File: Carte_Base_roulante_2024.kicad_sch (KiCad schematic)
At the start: 64 parts, among them J11 ENCA, J16 ALIM, J4 ENCB, J5 ENCC, Q2 IRF7424, U1 STM32G484RETx

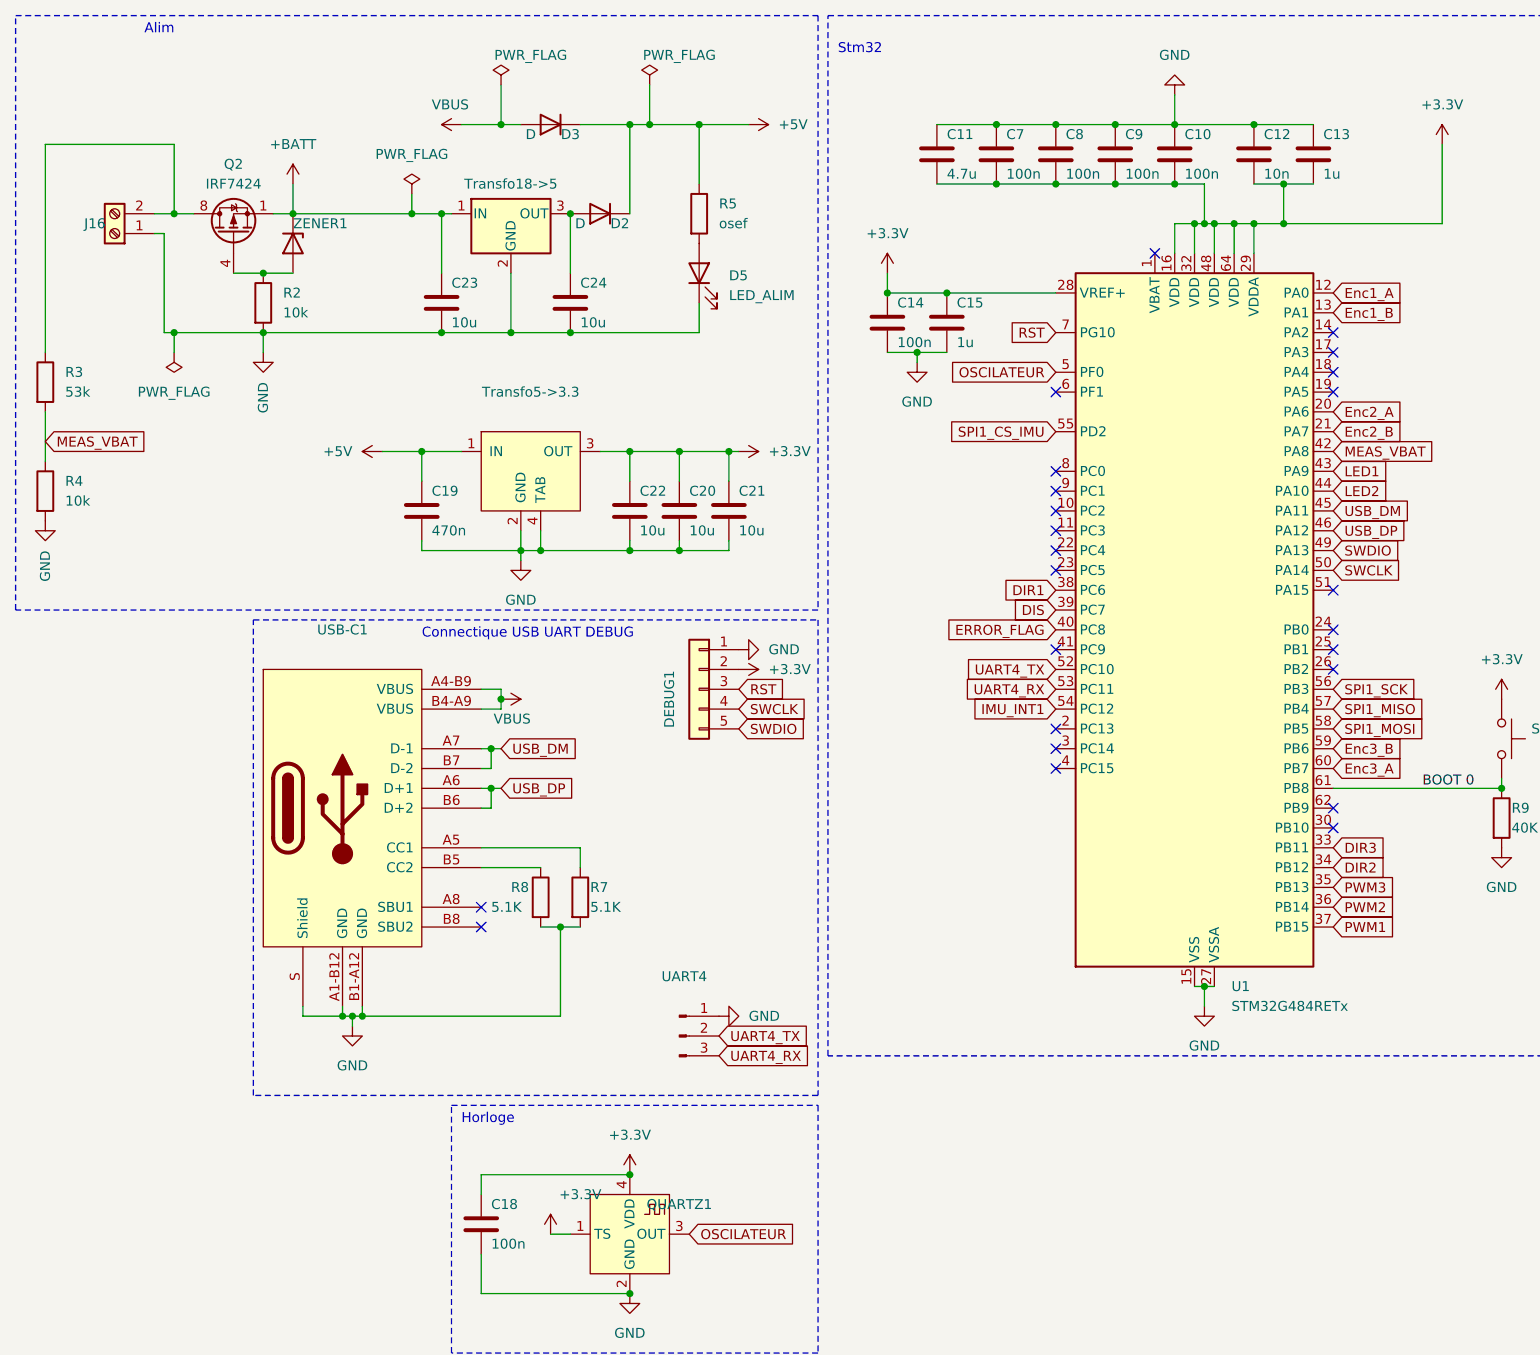
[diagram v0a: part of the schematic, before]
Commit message: routage avançé
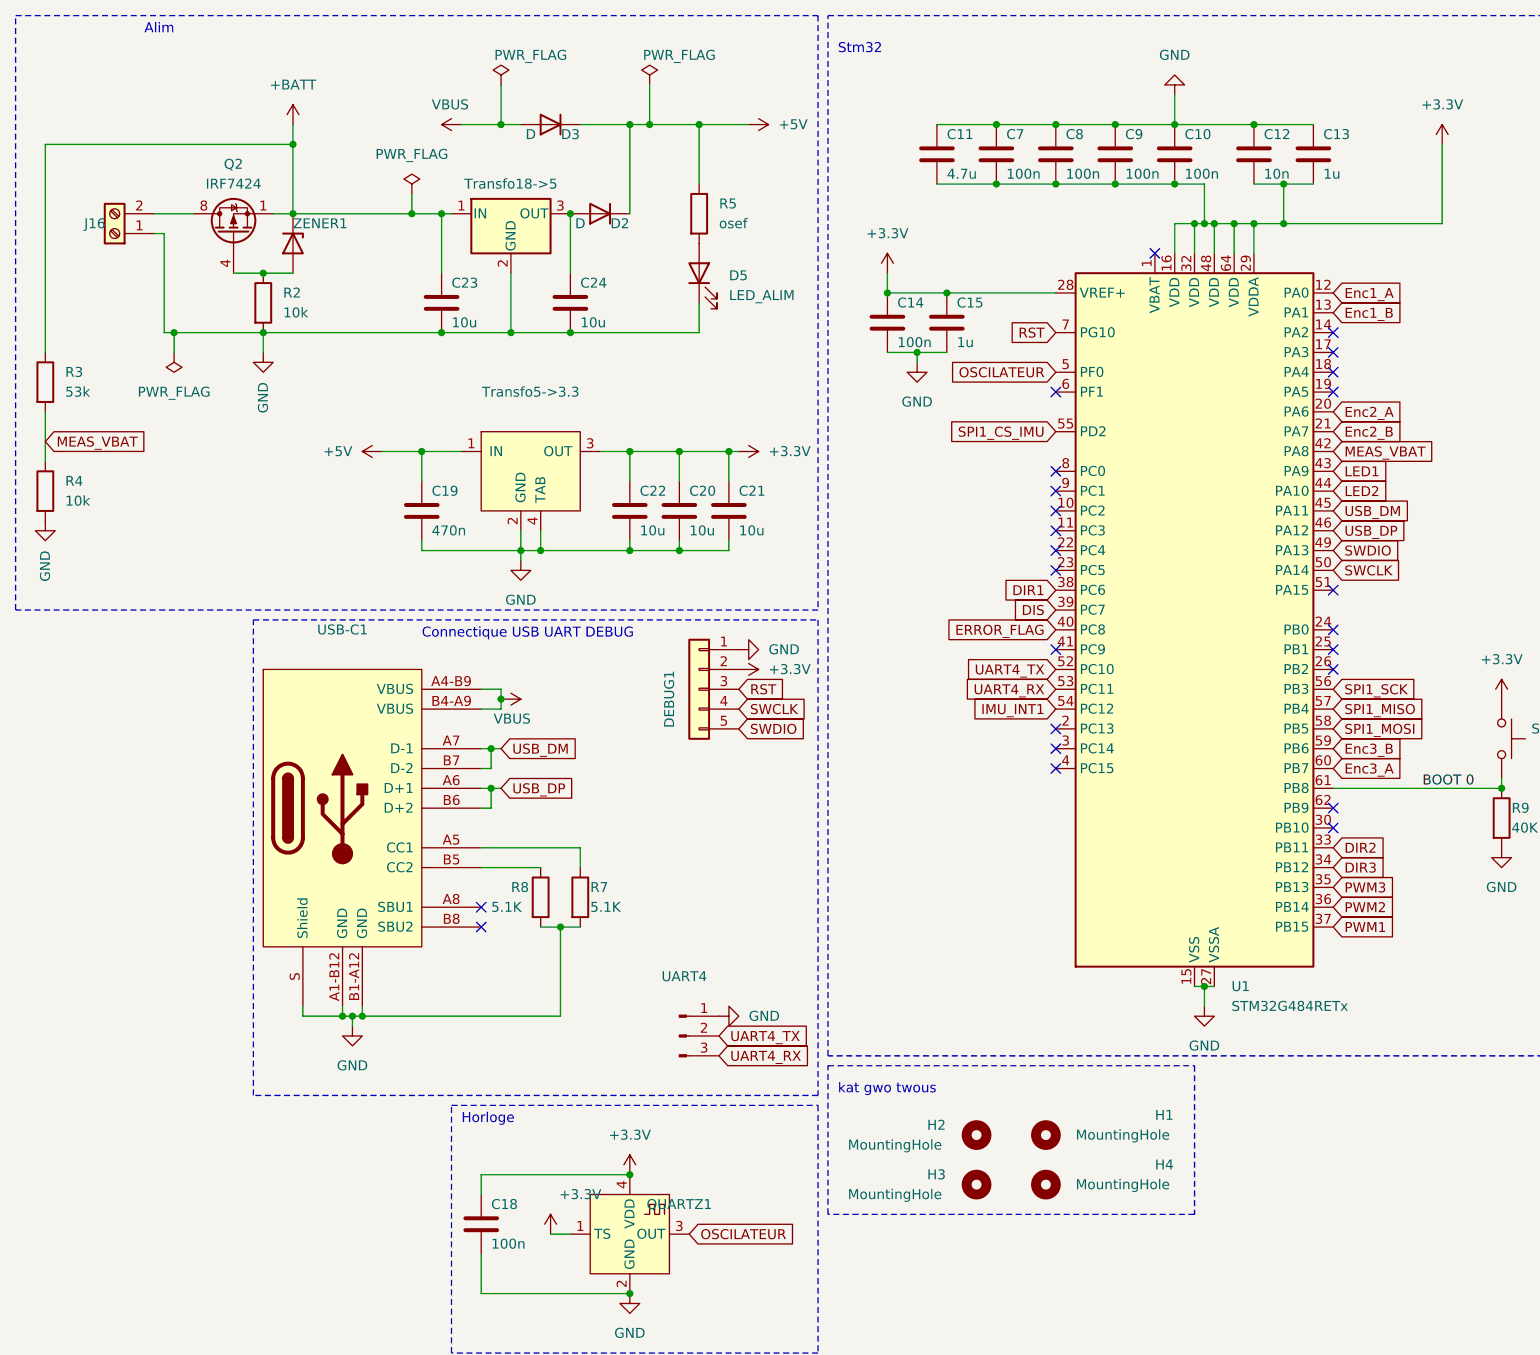
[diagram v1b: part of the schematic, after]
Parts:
- added H1, H2, H3, H4: MountingHole, MountingHole:MountingHole_3.2mm_M3, symbol Mechanical:MountingHole
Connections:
- net +BATT: now also R3.1
- net DIR2: now also U1.33 (PB11); no longer U1.34 (PB12)
- net DIR3: now also U1.34 (PB12); no longer U1.33 (PB11)
- net at J16.2 (Pin_2), Q2.5 (D), Q2.6 (D)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: no longer R3.1
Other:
- note added: "kat gwo twous"
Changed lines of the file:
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@@
   (junction (at 173.99 45.72) (diameter 0) (color 0 0 0 0)
   )
-  (junction (at 35.56 44.45) (diameter 0) (color 0 0 0 0)
-  )
   (junction (at 93.98 167.64) (diameter 0) (color 0 0 0 0)
   )
@@
   (junction (at 336.55 29.21) (diameter 0) (color 0 0 0 0)
   )
+  (junction (at 50.8 35.56) (diameter 0) (color 0 0 0 0)
+  )
   (junction (at 93.98 182.88) (diameter 0) (color 0 0 0 0)
   )
@@
     (stroke (width 0) (type default))
   )
+  (wire (pts (xy 19.05 35.56) (xy 50.8 35.56))
+    (stroke (width 0) (type default))
+  )
   (wire (pts (xy 86.36 44.45) (xy 86.36 52.07))
     (stroke (width 0) (type default))
@@
     (stroke (width 0) (type default))
   )
-  (wire (pts (xy 35.56 44.45) (xy 38.1 44.45))
+  (wire (pts (xy 33.02 44.45) (xy 38.1 44.45))
     (stroke (width 0) (type default))
   )
@@
     (stroke (width 0) (type default))
   )
-  (wire (pts (xy 19.05 35.56) (xy 35.56 35.56))
-    (stroke (width 0) (type default))
-  )
   (wire (pts (xy 254 36.83) (xy 255.27 36.83))
     (stroke (width 0) (type default))
@@
     (stroke (width 0) (type default))
   )
-  (wire (pts (xy 35.56 35.56) (xy 35.56 44.45))
-    (stroke (width 0) (type default))
-  )
   (wire (pts (xy 311.15 57.15) (xy 307.34 57.15))
     (stroke (width 0) (type default))
@@
     (stroke (width 0) (type default))
   )
+  (wire (pts (xy 50.8 35.56) (xy 50.8 44.45))
+    (stroke (width 0) (type default))
+  )
+  (wire (pts (xy 19.05 62.23) (xy 19.05 35.56))
+    (stroke (width 0) (type default))
+  )
   (wire (pts (xy 336.55 127) (xy 346.71 127))
     (stroke (width 0) (type default))
@@
     (stroke (width 0) (type default))
   )
-  (wire (pts (xy 33.02 44.45) (xy 35.56 44.45))
-    (stroke (width 0) (type default))
-  )
   (wire (pts (xy 163.83 45.72) (xy 166.37 45.72))
     (stroke (width 0) (type default))
@@
     (stroke (width 0) (type default))
   )
-  (wire (pts (xy 50.8 40.64) (xy 50.8 44.45))
+  (wire (pts (xy 50.8 33.02) (xy 50.8 35.56))
     (stroke (width 0) (type default))
   )
@@
     (stroke (width 0) (type default))
   )
-  (wire (pts (xy 19.05 35.56) (xy 19.05 62.23))
-    (stroke (width 0) (type default))
-  )
   (wire (pts (xy 177.8 45.72) (xy 173.99 45.72))
     (stroke (width 0) (type default))
@@
     (fill (type none))
   )
+  (rectangle (start 119.38 153.67) (end 166.37 172.72)
+    (stroke (width 0) (type dash))
+    (fill (type none))
+  )
   (rectangle (start 220.98 101.6) (end 283.21 130.81)
     (stroke (width 0) (type dash))
@@
     (effects (font (size 2 2)) (justify left bottom))
   )
+  (text "kat gwo twous\n" (at 120.65 157.48 0)
+    (effects (font (size 1.27 1.27)) (justify left bottom))
+  )
   (text "Encodeurs Moteurs" (at 222.25 81.28 0)
     (effects (font (size 1.27 1.27)) (justify left bottom))
@@
     )
   )
-  (global_label "DIR3" (shape input) (at 184.15 125.73 0) (fields_autoplaced)
+  (global_label "DIR3" (shape input) (at 184.15 128.27 0) (fields_autoplaced)
     (effects (font (size 1.27 1.27)) (justify left))
-    (property "Intersheetrefs" "${INTERSHEET_REFS}" (at 191.4895 125.73 0)
+    (property "Intersheetrefs" "${INTERSHEET_REFS}" (at 191.4895 128.27 0)
       (effects (font (size 1.27 1.27)) (justify left) hide)
     )
@@
     )
   )
-  (global_label "DIR2" (shape input) (at 184.15 128.27 0) (fields_autoplaced)
+  (global_label "DIR2" (shape input) (at 184.15 125.73 0) (fields_autoplaced)
     (effects (font (size 1.27 1.27)) (justify left))
-    (property "Intersheetrefs" "${INTERSHEET_REFS}" (at 191.4895 128.27 0)
+    (property "Intersheetrefs" "${INTERSHEET_REFS}" (at 191.4895 125.73 0)
       (effects (font (size 1.27 1.27)) (justify left) hide)
     )
@@
     )
   )
+  (symbol (lib_id "Mechanical:MountingHole") (at 147.32 168.91 0) (unit 1)
+    (in_bom yes) (on_board yes) (dnp no)
+    (property "Reference" "H4" (at 161.29 166.37 0)
+      (effects (font (size 1.27 1.27)) (justify left))
+    )
+    (property "Value" "MountingHole" (at 151.13 168.91 0)
+      (effects (font (size 1.27 1.27)) (justify left))
+    )
+    (property "Footprint" "MountingHole:MountingHole_3.2mm_M3" (at 147.32 168.91 0)
+      (effects (font (size 1.27 1.27)) hide)
+    )
+    (property "Datasheet" "~" (at 147.32 168.91 0)
+      (effects (font (size 1.27 1.27)) hide)
+    )
+    (instances
+      (project "Carte_Base_roulante_2024"
+        (path "/f941aee9-3a44-439b-9c30-032c53e86031"
+          (reference "H4") (unit 1)
+        )
+      )
+    )
+  )
   (symbol (lib_id "power:+5V") (at 231.14 90.17 90) (mirror x) (unit 1)
     (in_bom yes) (on_board yes) (dnp no) (fields_autoplaced)
@@
     )
   )
+  (symbol (lib_id "Mechanical:MountingHole") (at 147.32 162.56 0) (unit 1)
+    (in_bom yes) (on_board yes) (dnp no)
+    (property "Reference" "H1" (at 161.29 160.02 0)
+      (effects (font (size 1.27 1.27)) (justify left))
+    )
+    (property "Value" "MountingHole" (at 151.13 162.56 0)
+      (effects (font (size 1.27 1.27)) (justify left))
+    )
+    (property "Footprint" "MountingHole:MountingHole_3.2mm_M3" (at 147.32 162.56 0)
+      (effects (font (size 1.27 1.27)) hide)
+    )
+    (property "Datasheet" "~" (at 147.32 162.56 0)
+      (effects (font (size 1.27 1.27)) hide)
+    )
+    (instances
+      (project "Carte_Base_roulante_2024"
+        (path "/f941aee9-3a44-439b-9c30-032c53e86031"
+          (reference "H1") (unit 1)
+        )
+      )
+    )
+  )
   (symbol (lib_id "Device:C") (at 67.31 82.55 0) (unit 1)
     (in_bom yes) (on_board yes) (dnp no)
@@
     )
   )
-  (symbol (lib_id "power:+BATT") (at 50.8 40.64 0) (unit 1)
+  (symbol (lib_id "power:+BATT") (at 50.8 33.02 0) (unit 1)
     (in_bom yes) (on_board yes) (dnp no) (fields_autoplaced)
-    (property "Reference" "#PWR029" (at 50.8 44.45 0)
+    (property "Reference" "#PWR029" (at 50.8 36.83 0)
       (effects (font (size 1.27 1.27)) hide)
     )
-    (property "Value" "+BATT" (at 50.8 35.56 0)
+    (property "Value" "+BATT" (at 50.8 27.94 0)
       (effects (font (size 1.27 1.27)))
     )
-    (property "Footprint" "" (at 50.8 40.64 0)
+    (property "Footprint" "" (at 50.8 33.02 0)
       (effects (font (size 1.27 1.27)) hide)
     )
-    (property "Datasheet" "" (at 50.8 40.64 0)
+    (property "Datasheet" "" (at 50.8 33.02 0)
       (effects (font (size 1.27 1.27)) hide)
     )
@@
     )
   )
+  (symbol (lib_id "Mechanical:MountingHole") (at 138.43 162.56 0) (unit 1)
+    (in_bom yes) (on_board yes) (dnp no)
+    (property "Reference" "H2" (at 132.08 161.29 0)
+      (effects (font (size 1.27 1.27)) (justify left))
+    )
+    (property "Value" "MountingHole" (at 121.92 163.83 0)
+      (effects (font (size 1.27 1.27)) (justify left))
+    )
+    (property "Footprint" "MountingHole:MountingHole_3.2mm_M3" (at 138.43 162.56 0)
+      (effects (font (size 1.27 1.27)) hide)
+    )
+    (property "Datasheet" "~" (at 138.43 162.56 0)
+      (effects (font (size 1.27 1.27)) hide)
+    )
+    (instances
+      (project "Carte_Base_roulante_2024"
+        (path "/f941aee9-3a44-439b-9c30-032c53e86031"
+          (reference "H2") (unit 1)
+        )
+      )
+    )
+  )
   (symbol (lib_id "power:PWR_FLAG") (at 35.56 62.23 180) (unit 1)
     (in_bom yes) (on_board yes) (dnp no) (fields_autoplaced)
@@
         )
       )
+    )
+  )
+  (symbol (lib_id "Mechanical:MountingHole") (at 138.43 168.91 0) (unit 1)
+    (in_bom yes) (on_board yes) (dnp no)
+    (property "Reference" "H3" (at 132.08 167.64 0)
+      (effects (font (size 1.27 1.27)) (justify left))
+    )
+    (property "Value" "MountingHole" (at 121.92 170.18 0)
+      (effects (font (size 1.27 1.27)) (justify left))
+    )
+    (property "Footprint" "MountingHole:MountingHole_3.2mm_M3" (at 138.43 168.91 0)
+      (effects (font (size 1.27 1.27)) hide)
+    )
+    (property "Datasheet" "~" (at 138.43 168.91 0)
+      (effects (font (size 1.27 1.27)) hide)
+    )
+    (instances
+      (project "Carte_Base_roulante_2024"
+        (path "/f941aee9-3a44-439b-9c30-032c53e86031"
+          (reference "H3") (unit 1)
+        )
+      )
